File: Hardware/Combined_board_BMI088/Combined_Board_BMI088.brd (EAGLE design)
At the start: 47 x 132.1 mm, 19 parts, among them IC1 788TV, M1 SERVO, M2 SERVO

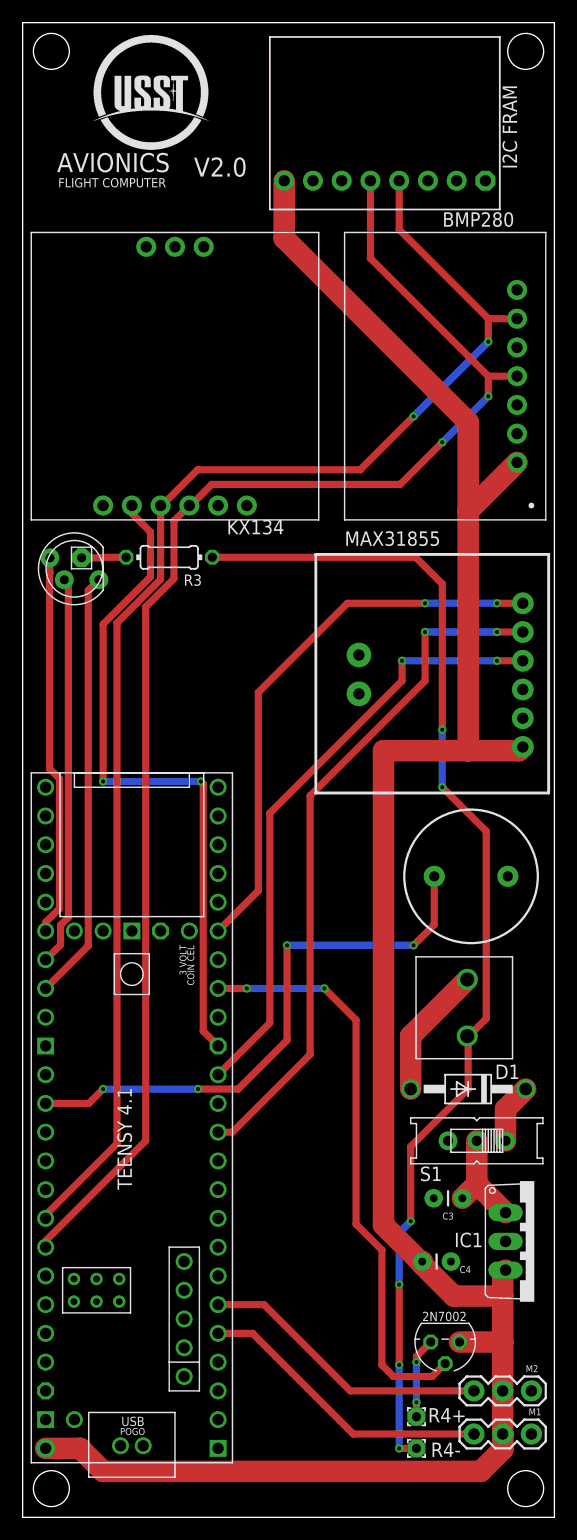
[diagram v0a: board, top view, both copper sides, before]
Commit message: Updated flight computer to new version for mini rockets
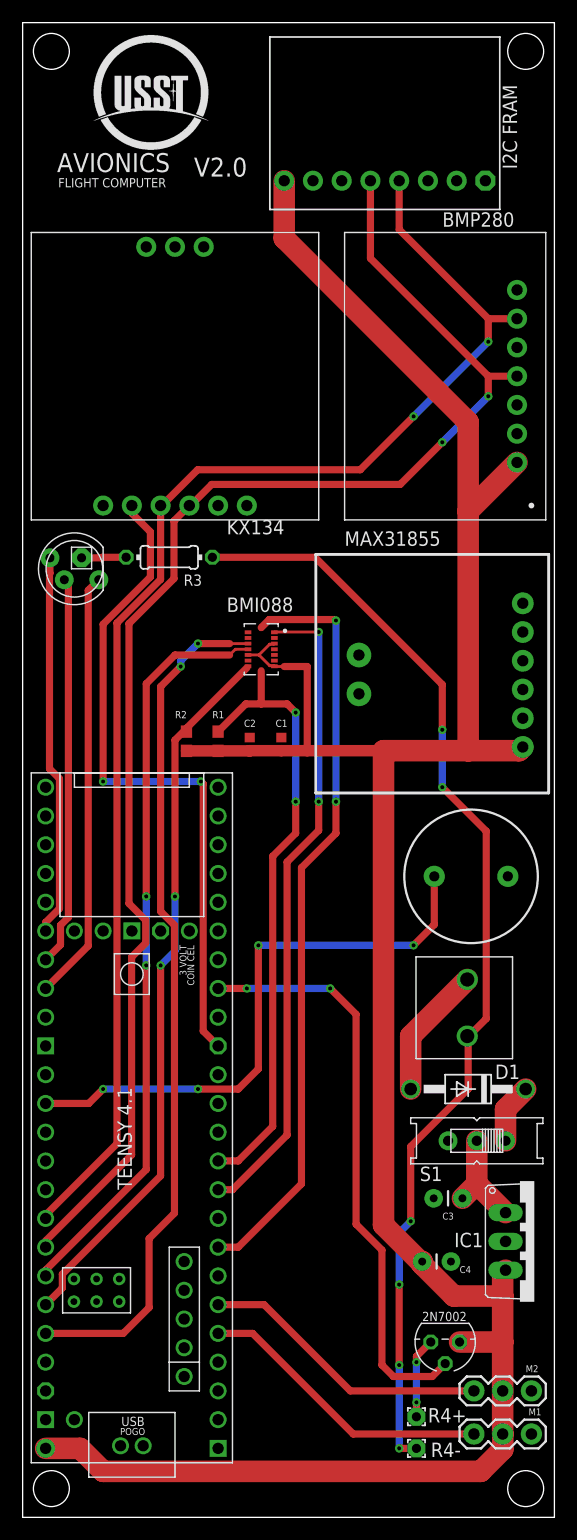
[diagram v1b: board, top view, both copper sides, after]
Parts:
- added C1, C2: 0.1uF, SparkFun-Capacitors:0402
- added R1, R2: 0.1, SparkFun-Resistors:0603
- added U1: BMI088, BMI088:PQFN50P450X300X100-16N
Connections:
- net 5V: now also C1.1, C2.1, R1.1, R2.1, U1.11, U1.3, U1.7
- net GND: now also C1.2, C2.2, U1.2, U1.4, U1.6
- net HEADER2: now also U1.16
- net HEADER4: now also U1.1
- net HEADER5: now also R1.2, U1.8
- net HEADER6: now also U1.12
- net HEADER7: now also R2.2, U1.9
- net HEADER8: now also U1.13
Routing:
- net HEADER8: track 0.00 -> 76.2 mm, vias 0 -> 2
- net HEADER2: track 0.00 -> 67.7 mm, vias 0 -> 2
- net HEADER6: track 0.00 -> 66.3 mm, vias 0 -> 2
- net HEADER7: track 0.00 -> 64.1 mm, vias 0 -> 2
- net CS: track 61.2 -> 0.00 mm, vias 2 -> 0
- net HEADER4: track 0.00 -> 57.6 mm, vias 0 -> 2
- net HEADER5: track 0.00 -> 54.6 mm, vias 0 -> 2
- net MISO: track 54.0 -> 0.00 mm, vias 2 -> 0
- net CLK: track 49.2 -> 0.00 mm, vias 2 -> 0
- net 5V: track 192.6 -> 225.4 mm
- net GND: track 104.1 -> 98.9 mm
- net BUZZER: track 50.1 -> 51.6 mm
- net SCL: track 127.1 -> 128.3 mm
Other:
- board text added: "BMI088"
- board text added: "C1"
- board text added: "C2"
- board text added: "R1"
- board text added: "R2"
